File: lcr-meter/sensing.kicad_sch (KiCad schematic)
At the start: 33 parts, among them J4 Conn_01x04, U10 AMP03GPZ, U11 TMUX1101DCK, U12 TMUX1101DCK, U2 AMP03GPZ, U21 AMP03GPZ, U3 AMP03GPZ, U8 TMUX1101DCK, U9 TMUX1101DCK

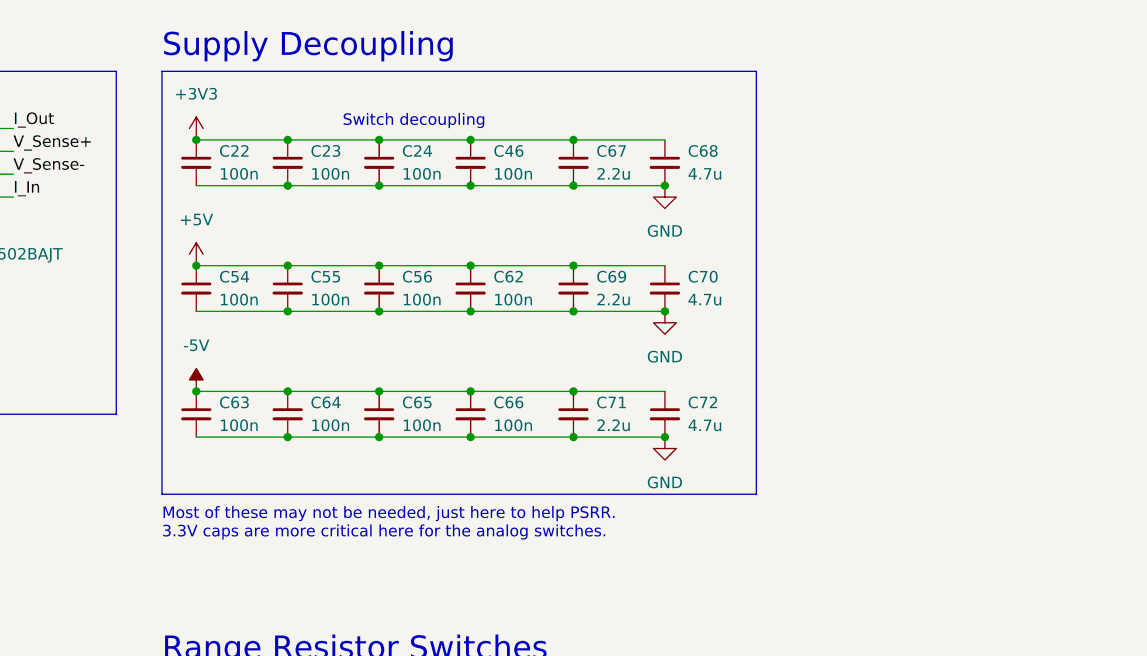
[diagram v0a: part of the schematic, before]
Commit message: Component grouping started
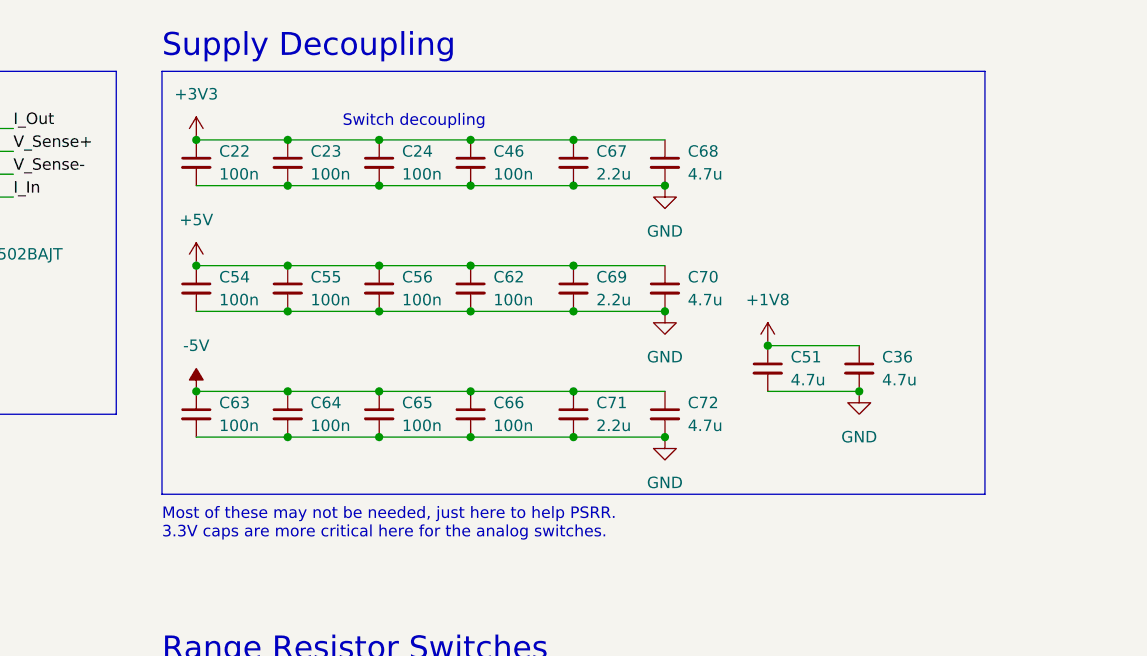
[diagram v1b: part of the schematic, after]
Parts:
- added C36, C51: 4.7u, Capacitor_SMD:C_0805_2012Metric, symbol Device:C_Small
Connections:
- net +1V8: now also C36.1, C51.1
- net GND: now also C36.2, C51.2

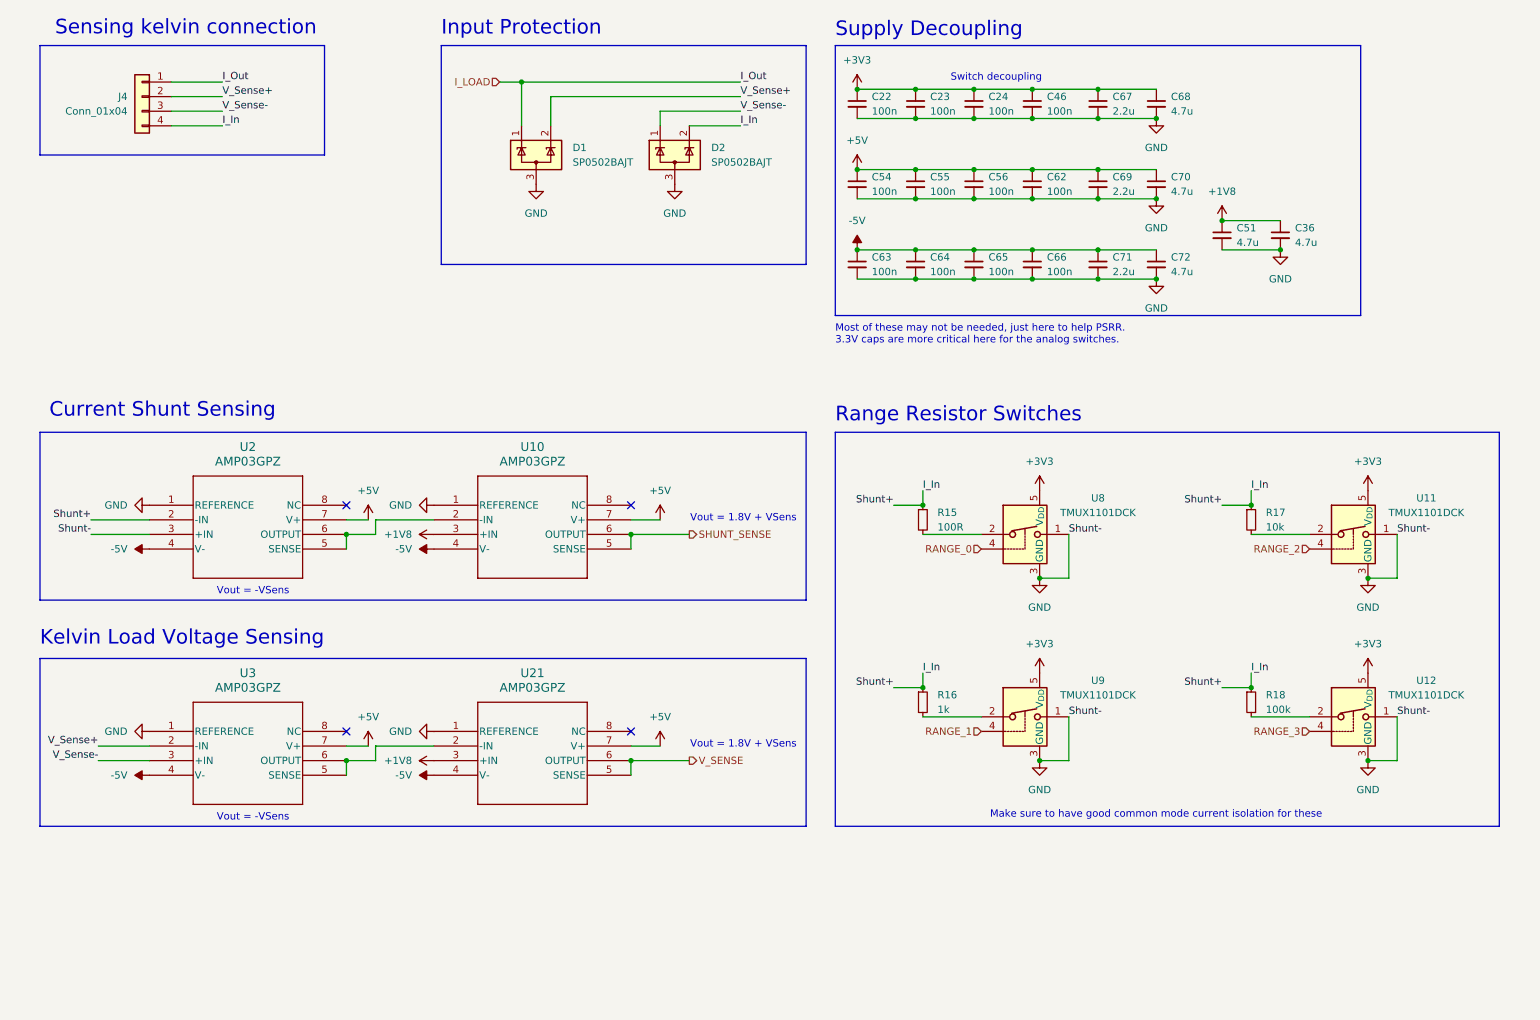
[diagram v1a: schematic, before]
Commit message: Rev A schematic fixes
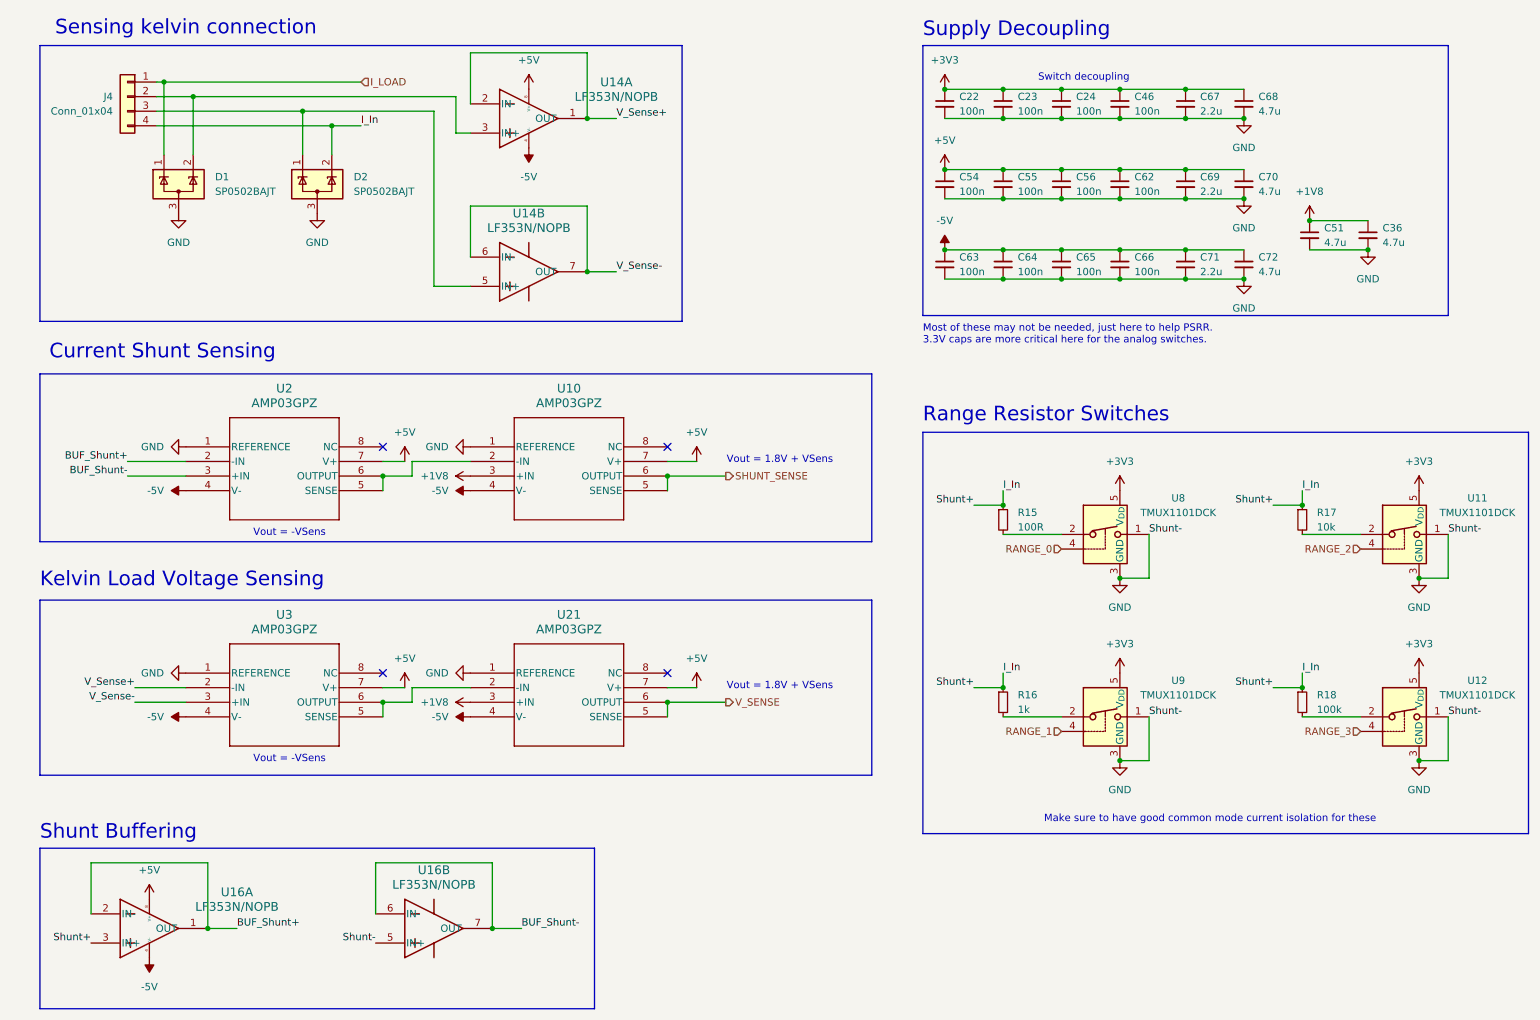
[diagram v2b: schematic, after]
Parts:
- added U14, U16: LF353N/NOPB, Package_DIP:DIP-8_W7.62mm, symbol 2024-10-13_18-48-05:LF353N_NOPB
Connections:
- net +5V: now also U14.8 (V+), U16.8 (V+)
- net -5V: now also U14.4 (V-), U16.4 (V-)
- net GND: now also U16.5 (IN+); no longer U2.3 (+IN)
- net I_In: now also U16.3 (IN+); no longer U2.2 (-IN)
- net V_Sense+: now also U14.1 (OUT), U14.2 (IN-); no longer D1.2 (K), J4.2 (Pin_2)
- net V_Sense-: now also U14.6 (IN-), U14.7 (OUT); no longer D2.1 (K), J4.3 (Pin_3)
- new net: D2.1 (K), J4.3 (Pin_3), U14.5 (IN+)
- new net: D1.2 (K), J4.2 (Pin_2), U14.3 (IN+)
- new net BUF_Shunt+: U16.1 (OUT), U16.2 (IN-), U2.2 (-IN)
- new net BUF_Shunt-: U16.6 (IN-), U16.7 (OUT), U2.3 (+IN)
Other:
- note added: "Shunt Buffering"
- note removed: "Input Protection"
- moved on the sheet: C22, C23, C24, C36, C46, C51, C54, C55, C56, C62, C63, C64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

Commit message: PCB updates
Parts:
- added C57, C58: 100n, Capacitor_SMD:C_0402_1005Metric, symbol Device:C_Small
- U11, U12, U8, U9: footprint Package_TO_SOT_SMD:SOT-23-5 -> Package_TO_SOT_SMD:SOT-353_SC-70-5
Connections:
- net +5V: now also C57.1
- net -5V: now also C58.1
- net GND: now also C57.2, C58.2
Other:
- moved on the sheet: C22, C23, C24, C36, C46, C51, C54, C55, C56, C62, C63, C64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

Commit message: Rev B Fixes
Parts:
- removed J4: Conn_01x04, Connector_PinHeader_2.54mm:PinHeader_1x04_P2.54mm_Vertical, symbol Connector_Generic:Conn_01x04
- added C59, C60: 100n, Capacitor_SMD:C_0402_1005Metric, symbol Device:C_Small
- added J7: Conn_01x04, Connector_PinHeader_2.54mm:PinHeader_1x04_P2.54mm_Vertical, symbol Connector_Generic:Conn_01x04
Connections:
- net +5V: now also C59.1
- net -5V: now also C60.1
- net GND: now also C59.2, C60.2
- net I_In: now also J7.4 (Pin_4)
- net I_LOAD: now also J7.1 (Pin_1)
- net BNCs/3: now reaches D2.1 (K), U14.5 (IN+)
- net BNCs/3: now also J7.3 (Pin_3)
- net BNCs/2: now reaches D1.2 (K), U14.3 (IN+)
- net BNCs/2: now also J7.2 (Pin_2)
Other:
- added sheet BNCs (BNCs.kicad_sch)
- moved on the sheet: D1, D2, U14A, U14B

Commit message: Polishing, Poster Creation
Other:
- moved on the sheet: C36, C51
